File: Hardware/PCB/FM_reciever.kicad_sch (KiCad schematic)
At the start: 0 parts

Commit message: added 2nd order bandpass
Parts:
- added AE1: Antenna, symbol Device:Antenna
- added C1, C2, C5, C6: C, symbol Device:C
- added R1, R2, R3, R4, R5, R6, R7, R8: R, symbol Device:R
- added U1, U2: ${SIM.PARAMS}, symbol Simulation_SPICE:OPAMP
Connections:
- new net: C6.2, R6.2, U2.1 (+)
- new net: R7.2, R8.1, U2.2 (-)
- new net: R1.1, U2.5
- new net: C1.1, R1.2, R3.1
- new net: C2.1, R3.2, U1.1 (+)
- new net: C1.2, R2.1
- new net: R2.2, R4.1, U1.2 (-)
- new net: R5.1, R7.1
- new net: C5.2, C6.1, R5.2
- new net: AE1.1 (A), C5.1
- new net GND: C2.2, R4.2, R6.1, R8.2

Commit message: mixer and bandpass worked out
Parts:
- added C5, C6, C7: C, symbol Device:C
- added D1: D_Schottky, symbol Device:D_Schottky
- added R10, R11, R12, R13: R, symbol Device:R
- added R9: 1k, symbol Device:R
- added U3: ${SIM.PARAMS}, symbol Simulation_SPICE:OPAMP
- C1: renamed from C5; value C -> 82p
- C2: renamed from C6; value C -> 82p
- C3: renamed from C1; value C -> 82p
- C4: renamed from C2; value C -> 82p
- R1: renamed from R5; value R -> 18
- R2: renamed from R6; value R -> 8
- R5: renamed from R1; value R -> 22
- R6: renamed from R3; value R -> 22
- renumbered R8 to R3, R7 to R4, R2 to R7, R4 to R8, U2 to U1, U1 to U2
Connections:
- net GND: now also R7.1, C7.2, R12.1; no longer R8.2
- net +5V: now reaches U1.3 (V+)
- net +5V: now also U2.3 (V+), R9.2, U3.3 (V+)
- net -5V: now reaches U1.4 (V-)
- net -5V: now also U2.4 (V-), U3.4 (V-)
- net at R5.1, U1.5: now also R1.1, R4.1
- net SCO_signal: now reaches C3.2
- net SCO_signal: now also R8.2, U2.5, D1.2 (A), R9.1; no longer R7.1
- new net: C5.2, D1.1 (K)
- new net: R12.2, R13.1, U3.2 (-)
- new net: C7.1, R11.2, U3.1 (+)
- new net: C6.1, R10.2, R11.1
- new net: C5.1, R10.1
- new net filterd_sig: C6.2, R13.2, U3.5
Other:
- note added: "Demodulator"
- note added: "FM bandpass filter"
- note added: "Low pass filter xHz"
- note added: "mixer"
- moved on the sheet: AE1, C1, C2, C3, C4, R1, R2, R3, R4, R5, R6, R7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

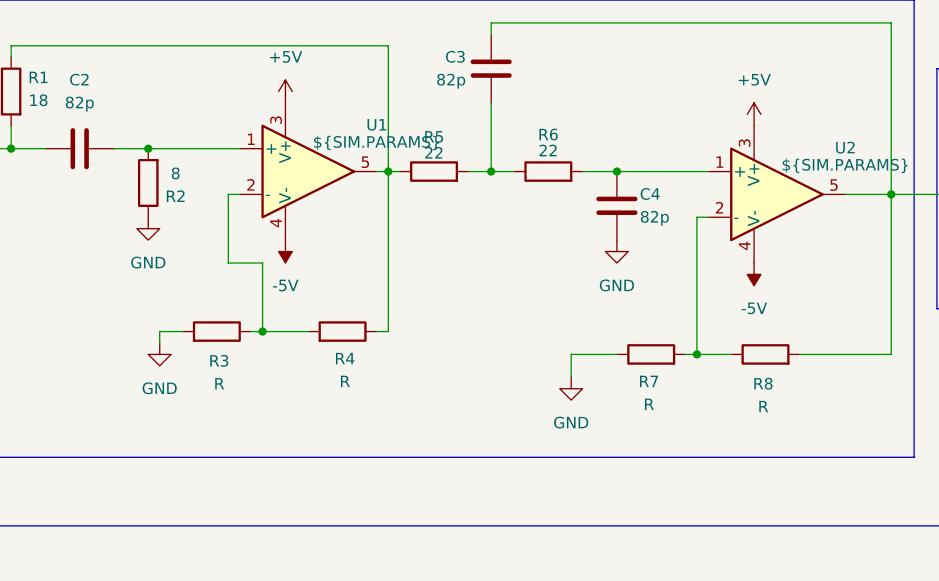
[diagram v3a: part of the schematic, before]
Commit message: added gain to filter
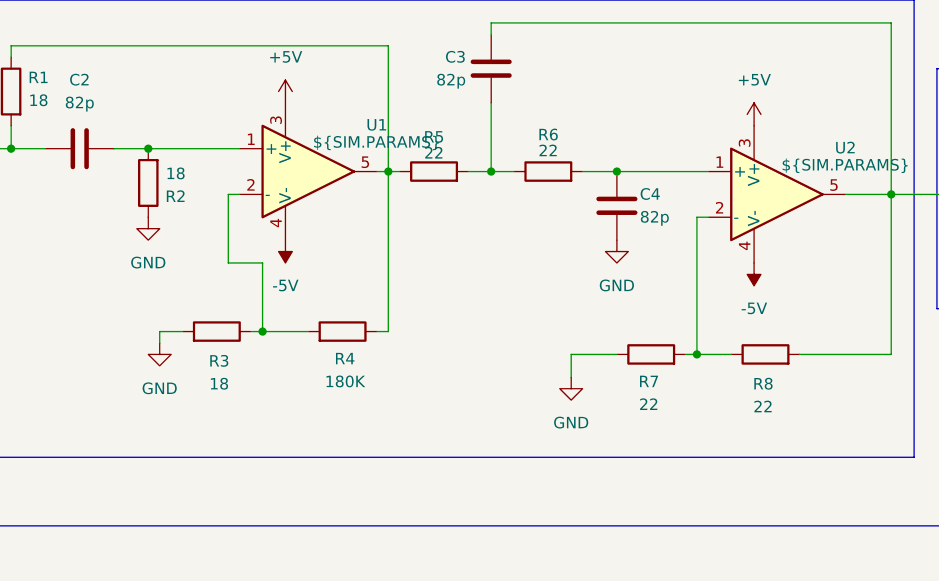
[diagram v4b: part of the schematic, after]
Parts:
- R2: value 8 -> 18
- R3: value R -> 18
- R4: value R -> 180K
- R7, R8: value R -> 22
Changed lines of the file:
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@@
 			)
 		)
-		(property "Value" "8"
+		(property "Value" "18"
 			(at 56.388 39.624 0)
 			(show_name no)
@@
 			)
 		)
-		(property "Value" "R"
+		(property "Value" "22"
 			(at 108.966 65.278 90)
 			(show_name no)
@@
 			)
 		)
-		(property "Value" "R"
+		(property "Value" "22"
 			(at 121.666 65.532 90)
 			(show_name no)
@@
 			)
 		)
-		(property "Value" "R"
+		(property "Value" "18"
 			(at 61.214 62.992 90)
 			(show_name no)
@@
 			)
 		)
-		(property "Value" "R"
+		(property "Value" "180K"
 			(at 75.184 62.738 90)
 			(show_name no)

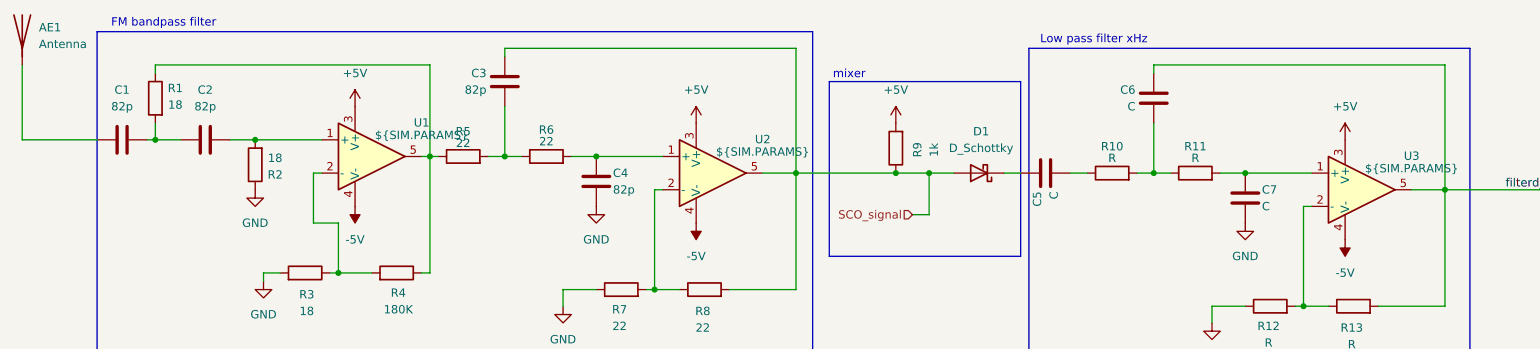
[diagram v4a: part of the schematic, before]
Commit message: adding power management
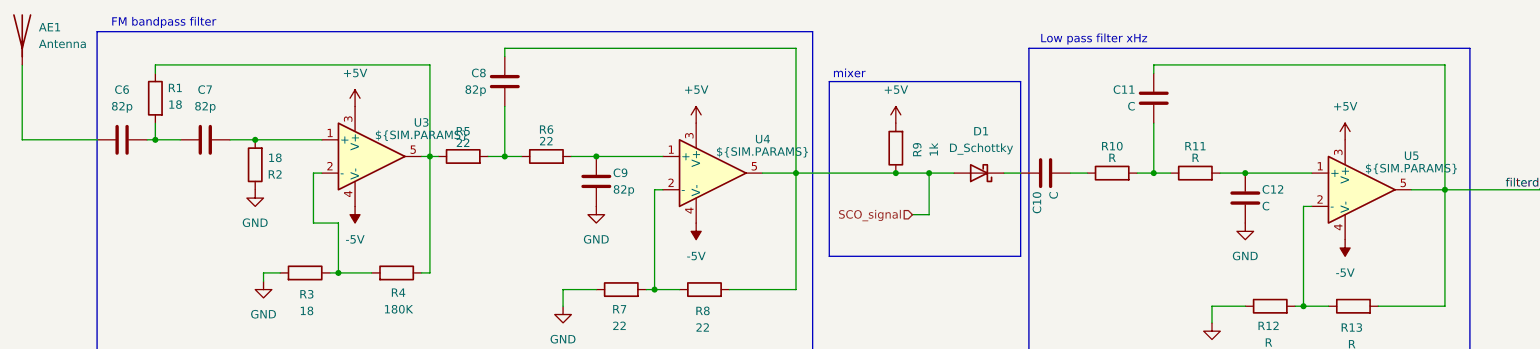
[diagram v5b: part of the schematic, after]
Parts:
- renumbered C5 to C10, C6 to C11, C7 to C12, C1 to C6, C2 to C7, C3 to C8, C4 to C9, U1 to U3, U2 to U4, U3 to U5
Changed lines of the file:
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@@
 		(dnp no)
 		(fields_autoplaced yes)
-		(property "Reference" "U1"
+		(property "Reference" "U3"
 			(at 78.74 34.2198 0)
 			(show_name no)
@@
 			(project "Radiowekker"
 				(path "/d1c96533-fea5-409f-9018-c843faf96bf8/7b2f9636-ff4a-4d39-ac0a-601e032c09a9"
-					(reference "U1")
+					(reference "U3")
 					(unit 1)
 				)
@@
 		(dnp no)
 		(fields_autoplaced yes)
-		(property "Reference" "#PWR09"
+		(property "Reference" "#PWR025"
 			(at 151.13 38.1 0)
 			(hide yes)
@@
 			(project "Radiowekker"
 				(path "/d1c96533-fea5-409f-9018-c843faf96bf8/7b2f9636-ff4a-4d39-ac0a-601e032c09a9"
-					(reference "#PWR09")
+					(reference "#PWR025")
 					(unit 1)
 				)
@@
 		(dnp no)
 		(fields_autoplaced yes)
-		(property "Reference" "#PWR010"
+		(property "Reference" "#PWR026"
 			(at 199.39 71.12 0)
 			(hide yes)
@@
 			(project "Radiowekker"
 				(path "/d1c96533-fea5-409f-9018-c843faf96bf8/7b2f9636-ff4a-4d39-ac0a-601e032c09a9"
-					(reference "#PWR010")
+					(reference "#PWR026")
 					(unit 1)
 				)
@@
 		(in_pos_files yes)
 		(dnp no)
-		(property "Reference" "C3"
+		(property "Reference" "C8"
 			(at 88.646 26.67 0)
 			(show_name no)
@@
 			(project "Radiowekker"
 				(path "/d1c96533-fea5-409f-9018-c843faf96bf8/7b2f9636-ff4a-4d39-ac0a-601e032c09a9"
-					(reference "C3")
+					(reference "C8")
 					(unit 1)
 				)
@@
 		(in_pos_files yes)
 		(dnp no)
-		(property "Reference" "C4"
+		(property "Reference" "C9"
 			(at 107.95 41.91 0)
 			(show_name no)
@@
 			(project "Radiowekker"
 				(path "/d1c96533-fea5-409f-9018-c843faf96bf8/7b2f9636-ff4a-4d39-ac0a-601e032c09a9"
-					(reference "C4")
+					(reference "C9")
 					(unit 1)
 				)
@@
 		(dnp no)
 		(fields_autoplaced yes)
-		(property "Reference" "#PWR011"
+		(property "Reference" "#PWR027"
 			(at 204.47 55.88 0)
 			(hide yes)
@@
 			(project "Radiowekker"
 				(path "/d1c96533-fea5-409f-9018-c843faf96bf8/7b2f9636-ff4a-4d39-ac0a-601e032c09a9"
-					(reference "#PWR011")
+					(reference "#PWR027")
 					(unit 1)
 				)
@@
 		(dnp no)
 		(fields_autoplaced yes)
-		(property "Reference" "U3"
+		(property "Reference" "U5"
 			(at 229.87 39.2998 0)
 			(show_name no)
@@
 			(project "Radiowekker"
 				(path "/d1c96533-fea5-409f-9018-c843faf96bf8/7b2f9636-ff4a-4d39-ac0a-601e032c09a9"
-					(reference "U3")
+					(reference "U5")
 					(unit 1)
 				)
@@
 		(dnp no)
 		(fields_autoplaced yes)
-		(property "Reference" "U2"
+		(property "Reference" "U4"
 			(at 130.81 36.7598 0)
 			(show_name no)
@@
 			(project "Radiowekker"
 				(path "/d1c96533-fea5-409f-9018-c843faf96bf8/7b2f9636-ff4a-4d39-ac0a-601e032c09a9"
-					(reference "U2")
+					(reference "U4")
 					(unit 1)
 				)
@@
 		(dnp no)
 		(fields_autoplaced yes)
-		(property "Reference" "#PWR05"
+		(property "Reference" "#PWR021"
 			(at 100.33 68.58 0)
 			(hide yes)
@@
 			(project "Radiowekker"
 				(path "/d1c96533-fea5-409f-9018-c843faf96bf8/7b2f9636-ff4a-4d39-ac0a-601e032c09a9"
-					(reference "#PWR05")
+					(reference "#PWR021")
 					(unit 1)
 				)
@@
 		(dnp no)
 		(fields_autoplaced yes)
-		(property "Reference" "#PWR04"
+		(property "Reference" "#PWR020"
 			(at 68.58 43.18 0)
 			(hide yes)
@@
 			(project "Radiowekker"
 				(path "/d1c96533-fea5-409f-9018-c843faf96bf8/7b2f9636-ff4a-4d39-ac0a-601e032c09a9"
-					(reference "#PWR04")
+					(reference "#PWR020")
 					(unit 1)
 				)
@@
 		(dnp no)
 		(fields_autoplaced yes)
-		(property "Reference" "#PWR013"
+		(property "Reference" "#PWR029"
 			(at 219.71 48.26 0)
 			(hide yes)
@@
 			(project "Radiowekker"
 				(path "/d1c96533-fea5-409f-9018-c843faf96bf8/7b2f9636-ff4a-4d39-ac0a-601e032c09a9"
-					(reference "#PWR013")
+					(reference "#PWR029")
 					(unit 1)
 				)
@@
 		(dnp no)
 		(fields_autoplaced yes)
-		(property "Reference" "#PWR06"
+		(property "Reference" "#PWR022"
 			(at 105.41 53.34 0)
 			(hide yes)
@@
 			(project "Radiowekker"
 				(path "/d1c96533-fea5-409f-9018-c843faf96bf8/7b2f9636-ff4a-4d39-ac0a-601e032c09a9"
-					(reference "#PWR06")
+					(reference "#PWR022")
 					(unit 1)
 				)
@@
 		(in_pos_files yes)
 		(dnp no)
-		(property "Reference" "C7"
+		(property "Reference" "C12"
 			(at 207.01 44.45 0)
 			(show_name no)
@@
 			(project "Radiowekker"
 				(path "/d1c96533-fea5-409f-9018-c843faf96bf8/7b2f9636-ff4a-4d39-ac0a-601e032c09a9"
-					(reference "C7")
+					(reference "C12")
 					(unit 1)
 				)
@@
 		(dnp no)
 		(fields_autoplaced yes)
-		(property "Reference" "#PWR03"
+		(property "Reference" "#PWR019"
 			(at 68.58 35.56 0)
 			(hide yes)
@@
 			(project "Radiowekker"
 				(path "/d1c96533-fea5-409f-9018-c843faf96bf8/7b2f9636-ff4a-4d39-ac0a-601e032c09a9"
-					(reference "#PWR03")
+					(reference "#PWR019")
 					(unit 1)
 				)
@@
 		(dnp no)
 		(fields_autoplaced yes)
-		(property "Reference" "#PWR02"
+		(property "Reference" "#PWR018"
 			(at 54.61 64.77 0)
 			(hide yes)
@@
 			(project "Radiowekker"
 				(path "/d1c96533-fea5-409f-9018-c843faf96bf8/7b2f9636-ff4a-4d39-ac0a-601e032c09a9"
-					(reference "#PWR02")
+					(reference "#PWR018")
 					(unit 1)
 				)
@@
 		(dnp no)
 		(fields_autoplaced yes)
-		(property "Reference" "#PWR012"
+		(property "Reference" "#PWR028"
 			(at 219.71 40.64 0)
 			(hide yes)
@@
 			(project "Radiowekker"
 				(path "/d1c96533-fea5-409f-9018-c843faf96bf8/7b2f9636-ff4a-4d39-ac0a-601e032c09a9"
-					(reference "#PWR012")
+					(reference "#PWR028")
 					(unit 1)
 				)
@@
 		(dnp no)
 		(fields_autoplaced yes)
-		(property "Reference" "#PWR07"
+		(property "Reference" "#PWR023"
 			(at 120.65 38.1 0)
 			(hide yes)
@@
 			(project "Radiowekker"
 				(path "/d1c96533-fea5-409f-9018-c843faf96bf8/7b2f9636-ff4a-4d39-ac0a-601e032c09a9"
-					(reference "#PWR07")
+					(reference "#PWR023")
 					(unit 1)
 				)
@@
 		(dnp no)
 		(fields_autoplaced yes)
-		(property "Reference" "C2"
+		(property "Reference" "C7"
 			(at 45.72 29.21 90)
 			(show_name no)
@@
 			(project "Radiowekker"
 				(path "/d1c96533-fea5-409f-9018-c843faf96bf8/7b2f9636-ff4a-4d39-ac0a-601e032c09a9"
-					(reference "C2")
+					(reference "C7")
 					(unit 1)
 				)
@@
 		(in_pos_files yes)
 		(dnp no)
-		(property "Reference" "C5"
+		(property "Reference" "C10"
 			(at 172.72 44.704 0)
 			(show_name no)
@@
 			(project "Radiowekker"
 				(path "/d1c96533-fea5-409f-9018-c843faf96bf8/7b2f9636-ff4a-4d39-ac0a-601e032c09a9"
-					(reference "C5")
+					(reference "C10")
 					(unit 1)
 				)
@@
 		(dnp no)
 		(fields_autoplaced yes)
-		(property "Reference" "#PWR01"
+		(property "Reference" "#PWR017"
 			(at 53.34 50.8 0)
 			(hide yes)
@@
 			(project "Radiowekker"
 				(path "/d1c96533-fea5-409f-9018-c843faf96bf8/7b2f9636-ff4a-4d39-ac0a-601e032c09a9"
-					(reference "#PWR01")
+					(reference "#PWR017")
 					(unit 1)
 				)
@@
 		(in_pos_files yes)
 		(dnp no)
-		(property "Reference" "C6"
+		(property "Reference" "C11"
 			(at 187.706 29.21 0)
 			(show_name no)
@@
 			(project "Radiowekker"
 				(path "/d1c96533-fea5-409f-9018-c843faf96bf8/7b2f9636-ff4a-4d39-ac0a-601e032c09a9"
-					(reference "C6")
+					(reference "C11")
 					(unit 1)
 				)
@@
 		(dnp no)
 		(fields_autoplaced yes)
-		(property "Reference" "C1"
+		(property "Reference" "C6"
 			(at 33.02 29.21 90)
 			(show_name no)
@@
 			(project "Radiowekker"
 				(path "/d1c96533-fea5-409f-9018-c843faf96bf8/7b2f9636-ff4a-4d39-ac0a-601e032c09a9"
-					(reference "C1")
+					(reference "C6")
 					(unit 1)
 				)
@@
 		(dnp no)
 		(fields_autoplaced yes)
-		(property "Reference" "#PWR08"
+		(property "Reference" "#PWR024"
 			(at 120.65 45.72 0)
 			(hide yes)
@@
 			(project "Radiowekker"
 				(path "/d1c96533-fea5-409f-9018-c843faf96bf8/7b2f9636-ff4a-4d39-ac0a-601e032c09a9"
-					(reference "#PWR08")
-					(unit 1)
-				)
+					(reference "#PWR024")
+					(unit 1)
+				)

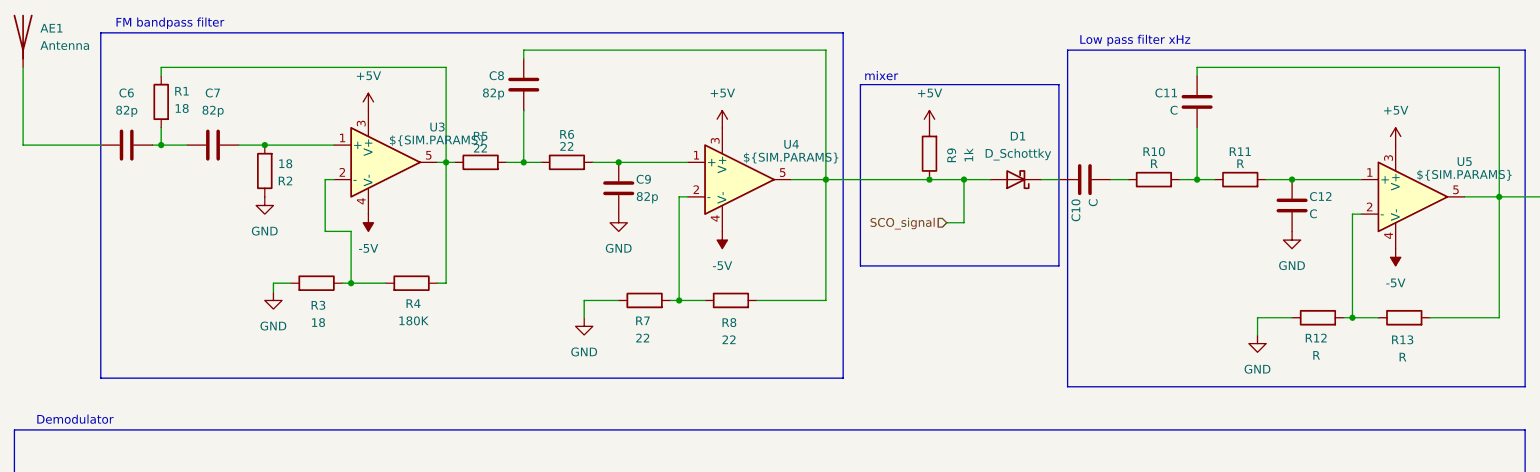
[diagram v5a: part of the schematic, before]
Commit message: added status LED's esd protection and new RGB symbol
Mass renumbering and library updates across KiCad schematics: updated many component Reference fields in Hardware/PCB/FM_reciever.kicad_sch and adjusted the project used_designators in Radiowekker.kicad_pro to match. Added a Device:LED symbol (with LED variants) to motherboard.kicad_sch and replaced the AP63203WU regulator symbol with a USBLC6-2SC6 power-protection symbol (updated footprint, datasheet, pins and graphics). Also added sym-lib-table and an RGB_leds symbol library. These changes keep designators consistent and introduce LED/ESD protection symbols for use in the PCB designs.
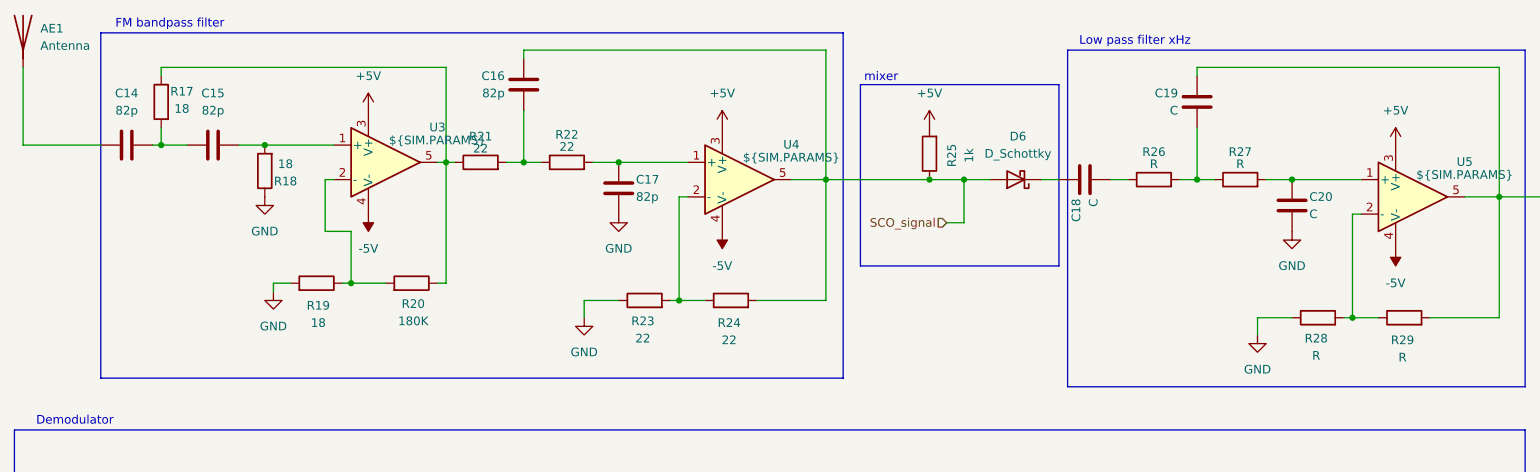
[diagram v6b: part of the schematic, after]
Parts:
- renumbered C6 to C14, C7 to C15, C8 to C16, C9 to C17, C10 to C18, C11 to C19, C12 to C20, D1 to D6, R1 to R17, R2 to R18, R3 to R19, R4 to R20, R5 to R21, R6 to R22, R7 to R23, R8 to R24, R9 to R25, R10 to R26, R11 to R27, R12 to R28, R13 to R29
